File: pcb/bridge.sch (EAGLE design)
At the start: 37 parts, among them IC1 MEGA8-AI, IC4 78L05SMD, IC5 LM358D

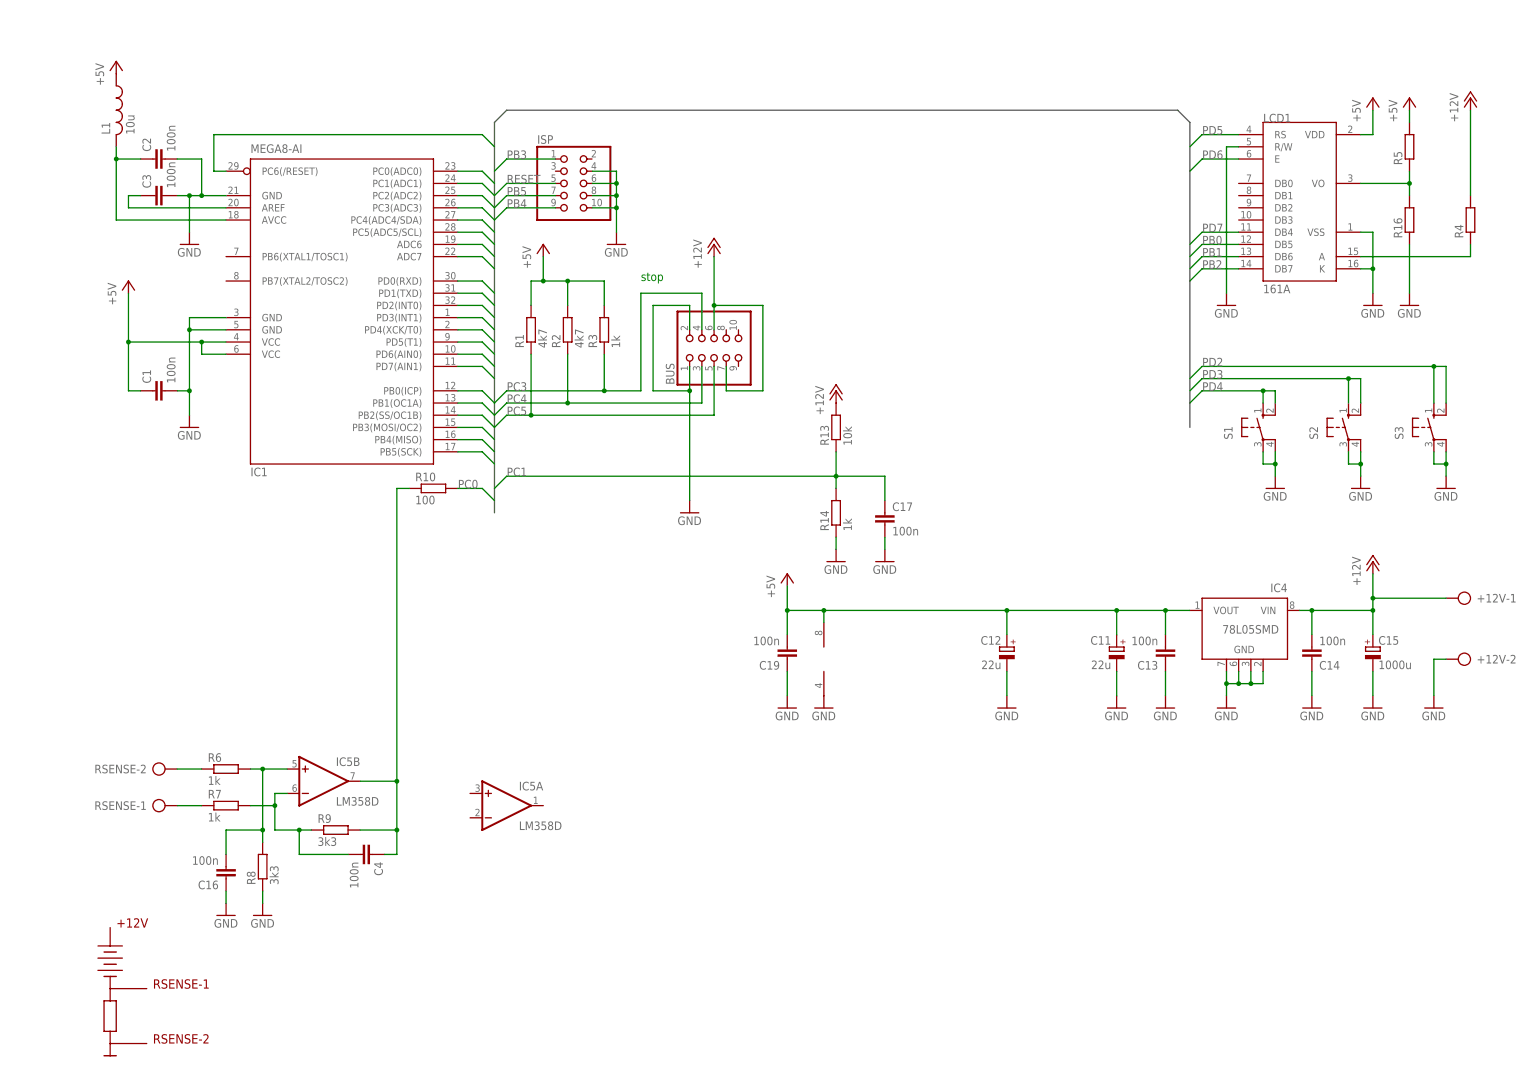
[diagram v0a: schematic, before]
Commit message: Bridge USB schematic.
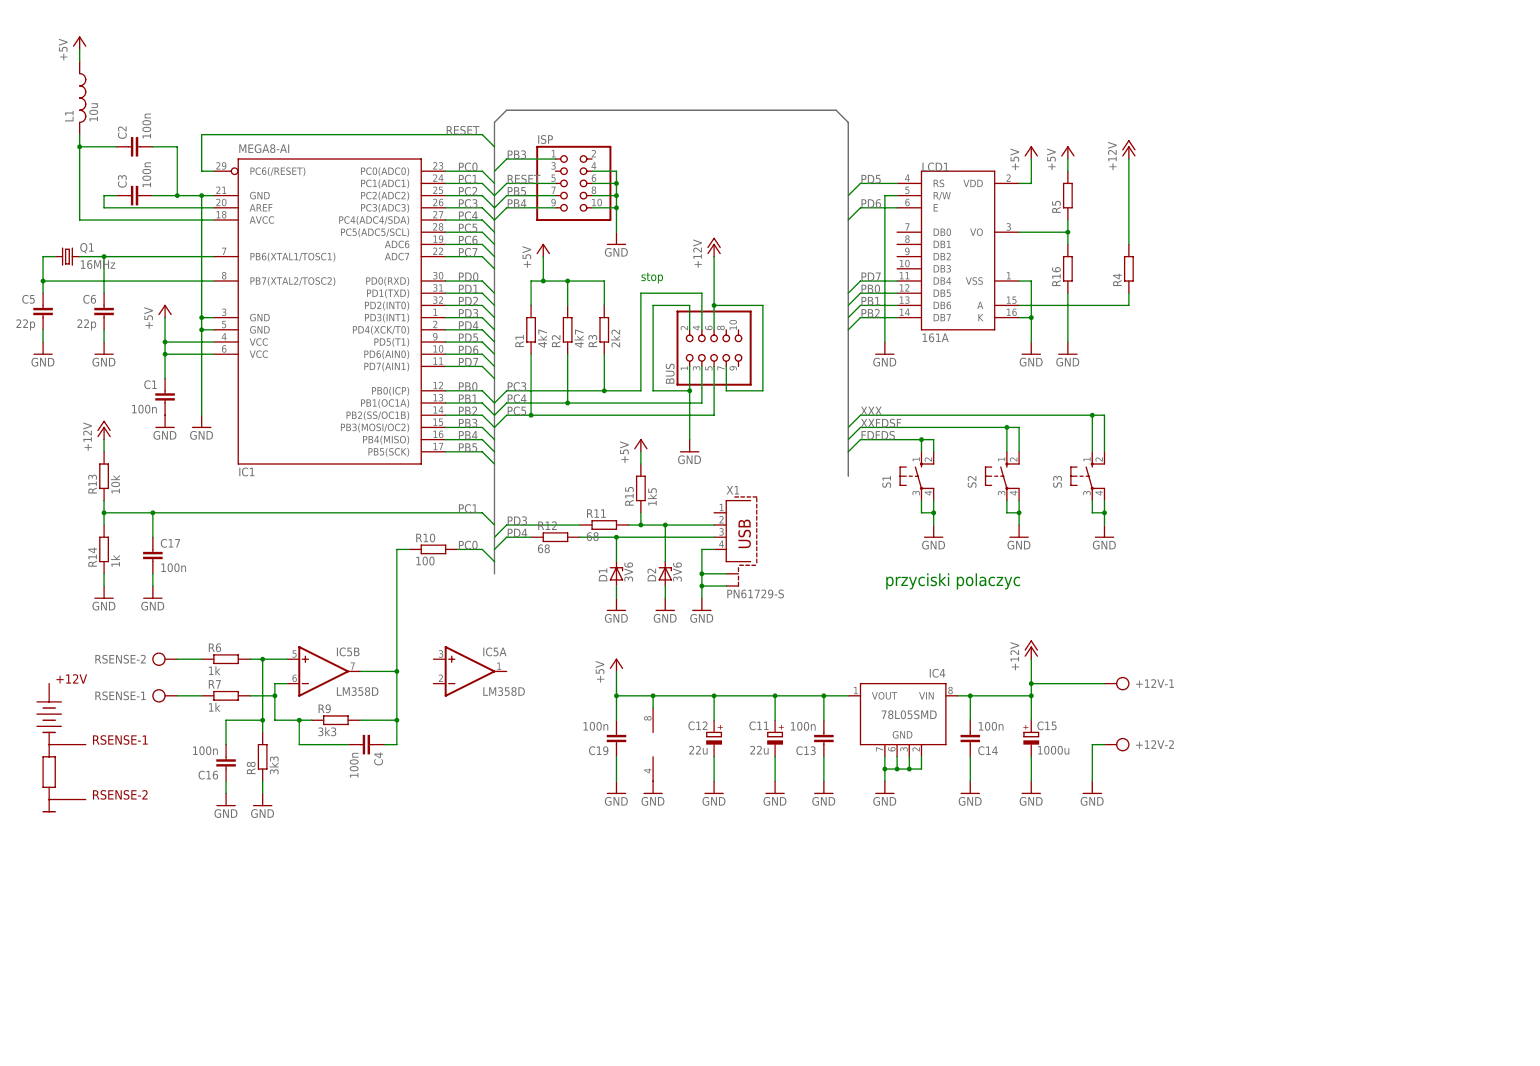
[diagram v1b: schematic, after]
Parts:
- added C5, C6: 22p, rcl:C-EUC1206
- added D1, D2: 3V6, diode:ZENER-DIODEDO34-7
- added Q1: 16MHz, crystal:CRYSTALHC49UP
- added R11, R12: 68, rcl:R-EU_M1206
- added R15: 1k5, rcl:R-EU_M1206
- added X1: PN61729-S, con-berg:PN61729-S
- R3: value 1k -> 2k2
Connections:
- new net FDFDS: S1.S, S1.S1
- new net N$11: C5.1, IC1.PB7(XTAL2/TOSC2), Q1.1
- new net N$5: D2.C, R11.2, R15.1, X1.2
- new net N$6: D1.C, R12.2, X1.3
- new net N$9: C6.1, IC1.PB6(XTAL1/TOSC1), Q1.2
- new net XXFDSF: S2.S, S2.S1
- new net XXX: S3.S, S3.S1
- net +5V: now also R15.2
- net GND: now also C5.2, C6.2, D1.A, D2.A, X1.4, X1.S1, X1.S2
- net PD2: no longer S3.S, S3.S1
- net PD3: now also R11.1; no longer S2.S, S2.S1
- net PD4: now also R12.1; no longer S1.S, S1.S1
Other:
- note added: "przyciski polaczyc"
- moved on the sheet: +12V-1, +12V-2, C1, C11, C12, C13, C14, C15, C16, C17, C19, C2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

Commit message: Bridge board ready.
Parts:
- removed C17: 100n, rcl:C-EUC1210
- added C7: 100n, rcl:C-EUC1206
- R4: device rcl:R-EU_R1218 -> rcl:R-EU_0207/12
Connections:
- removed net FDFDS: S1.S, S1.S1
- removed net XXFDSF: S2.S, S2.S1
- removed net XXX: S3.S, S3.S1
- net GND: now also C7.2; no longer C17.2
- net PC1: now also C7.1; no longer C17.1
- net PD0: now also S1.S, S1.S1
- net PD1: now also S2.S, S2.S1
- net PD2: now also S3.S, S3.S1
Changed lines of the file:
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@@
 <part name="GND13" library="supply1" deviceset="GND" device=""/>
 <part name="P+7" library="supply1" deviceset="+12V" device=""/>
-<part name="R4" library="rcl" deviceset="R-EU_" device="R1218"/>
 <part name="L1" library="rcl" deviceset="L-US" device="L1812" value="10u"/>
 <part name="IC4" library="linear" deviceset="78L*SMD" device="" technology="05"/>
@@
 <part name="P+8" library="supply1" deviceset="+5V" device=""/>
 <part name="C4" library="rcl" deviceset="C-EU" device="C1206" value="100n"/>
-<part name="C17" library="rcl" deviceset="C-EU" device="C1210" value="100n"/>
 <part name="GND5" library="supply1" deviceset="GND" device=""/>
 <part name="D1" library="diode" deviceset="ZENER-DIODE" device="DO34-7" value="3V6"/>
@@
 <part name="GND22" library="supply1" deviceset="GND" device=""/>
 <part name="GND8" library="supply1" deviceset="GND" device=""/>
+<part name="R4" library="rcl" deviceset="R-EU_" device="0207/12"/>
+<part name="C7" library="rcl" deviceset="C-EU" device="C1206" value="100n"/>
 </parts>
 <sheets>
@@
 <instance part="GND13" gate="1" x="208.28" y="0"/>
 <instance part="P+7" gate="1" x="213.36" y="81.28"/>
-<instance part="R4" gate="G$1" x="213.36" y="55.88" rot="R90"/>
 <instance part="L1" gate="G$1" x="-5.08" y="91.44"/>
 <instance part="IC4" gate="G$1" x="167.64" y="-33.02" rot="MR0"/>
@@
 <instance part="P+8" gate="1" x="200.66" y="81.28"/>
 <instance part="C4" gate="G$1" x="55.88" y="-43.18" rot="R270"/>
-<instance part="C17" gate="G$1" x="10.16" y="-2.54"/>
 <instance part="GND5" gate="1" x="10.16" y="-12.7"/>
 <instance part="D1" gate="G$1" x="106.68" y="-7.62" rot="R90"/>
@@
 <instance part="GND22" gate="1" x="0" y="38.1"/>
 <instance part="GND8" gate="1" x="12.7" y="22.86"/>
+<instance part="R4" gate="G$1" x="213.36" y="55.88" rot="R90"/>
+<instance part="C7" gate="G$1" x="10.16" y="-2.54"/>
 </instances>
 <busses>
@@
 <segment>
 <wire x1="10.16" y1="-7.62" x2="10.16" y2="-10.16" width="0.1524" layer="91"/>
-<pinref part="C17" gate="G$1" pin="2"/>
 <pinref part="GND5" gate="1" pin="GND"/>
+<pinref part="C7" gate="G$1" pin="2"/>
 </segment>
 <segment>
@@
 <wire x1="81.28" y1="2.54" x2="78.74" y2="5.08" width="0.1524" layer="91"/>
 <label x="73.66" y="5.08" size="1.778" layer="95"/>
-<pinref part="C17" gate="G$1" pin="1"/>
 <wire x1="10.16" y1="5.08" x2="10.16" y2="0" width="0.1524" layer="91"/>
 <pinref part="R13" gate="G$1" pin="1"/>
@@
 <wire x1="10.16" y1="5.08" x2="78.74" y2="5.08" width="0.1524" layer="91"/>
 <junction x="10.16" y="5.08"/>
+<pinref part="C7" gate="G$1" pin="1"/>
 </segment>
 </net>
@@
 <label x="73.66" y="53.34" size="1.778" layer="95"/>
 </segment>
+<segment>
+<wire x1="170.18" y1="17.78" x2="170.18" y2="20.32" width="0.1524" layer="91"/>
+<wire x1="170.18" y1="20.32" x2="172.72" y2="20.32" width="0.1524" layer="91"/>
+<wire x1="172.72" y1="20.32" x2="172.72" y2="17.78" width="0.1524" layer="91"/>
+<wire x1="170.18" y1="20.32" x2="157.48" y2="20.32" width="0.1524" layer="91"/>
+<wire x1="154.94" y1="17.78" x2="157.48" y2="20.32" width="0.1524" layer="91"/>
+<junction x="170.18" y="20.32"/>
+<label x="157.48" y="20.32" size="1.778" layer="95"/>
+<pinref part="S1" gate="1" pin="S"/>
+<pinref part="S1" gate="1" pin="S1"/>
+</segment>
 </net>
 <net name="PD1" class="0">
@@
 <label x="73.66" y="50.8" size="1.778" layer="95"/>
 </segment>
+<segment>
+<wire x1="190.5" y1="17.78" x2="190.5" y2="22.86" width="0.1524" layer="91"/>
+<wire x1="190.5" y1="22.86" x2="187.96" y2="22.86" width="0.1524" layer="91"/>
+<wire x1="187.96" y1="22.86" x2="187.96" y2="17.78" width="0.1524" layer="91"/>
+<wire x1="187.96" y1="22.86" x2="157.48" y2="22.86" width="0.1524" layer="91"/>
+<wire x1="154.94" y1="20.32" x2="157.48" y2="22.86" width="0.1524" layer="91"/>
+<junction x="187.96" y="22.86"/>
+<label x="157.48" y="22.86" size="1.778" layer="95"/>
+<pinref part="S2" gate="1" pin="S1"/>
+<pinref part="S2" gate="1" pin="S"/>
+</segment>
 </net>
 <net name="PD2" class="0">
@@
 <pinref part="IC1" gate="G$1" pin="PD2(INT0)"/>
 <label x="73.66" y="48.26" size="1.778" layer="95"/>
+</segment>
+<segment>
+<wire x1="205.74" y1="17.78" x2="205.74" y2="25.4" width="0.1524" layer="91"/>
+<wire x1="205.74" y1="25.4" x2="208.28" y2="25.4" width="0.1524" layer="91"/>
+<wire x1="208.28" y1="25.4" x2="208.28" y2="17.78" width="0.1524" layer="91"/>
+<wire x1="205.74" y1="25.4" x2="157.48" y2="25.4" width="0.1524" layer="91"/>
+<wire x1="154.94" y1="22.86" x2="157.48" y2="25.4" width="0.1524" layer="91"/>
+<junction x="205.74" y="25.4"/>
+<label x="157.48" y="25.4" size="1.778" layer="95"/>
+<pinref part="S3" gate="1" pin="S"/>
+<pinref part="S3" gate="1" pin="S1"/>
 </segment>
 </net>
@@
 </segment>
 </net>
-<net name="XXX" class="0">
-<segment>
-<wire x1="205.74" y1="17.78" x2="205.74" y2="25.4" width="0.1524" layer="91"/>
-<wire x1="205.74" y1="25.4" x2="208.28" y2="25.4" width="0.1524" layer="91"/>
-<wire x1="208.28" y1="25.4" x2="208.28" y2="17.78" width="0.1524" layer="91"/>
-<wire x1="205.74" y1="25.4" x2="157.48" y2="25.4" width="0.1524" layer="91"/>
-<wire x1="154.94" y1="22.86" x2="157.48" y2="25.4" width="0.1524" layer="91"/>
-<junction x="205.74" y="25.4"/>
-<label x="157.48" y="25.4" size="1.778" layer="95"/>
-<pinref part="S3" gate="1" pin="S"/>
-<pinref part="S3" gate="1" pin="S1"/>
-</segment>
-</net>
-<net name="XXFDSF" class="0">
-<segment>
-<wire x1="190.5" y1="17.78" x2="190.5" y2="22.86" width="0.1524" layer="91"/>
-<wire x1="190.5" y1="22.86" x2="187.96" y2="22.86" width="0.1524" layer="91"/>
-<wire x1="187.96" y1="22.86" x2="187.96" y2="17.78" width="0.1524" layer="91"/>
-<wire x1="187.96" y1="22.86" x2="157.48" y2="22.86" width="0.1524" layer="91"/>
-<wire x1="154.94" y1="20.32" x2="157.48" y2="22.86" width="0.1524" layer="91"/>
-<junction x="187.96" y="22.86"/>
-<label x="157.48" y="22.86" size="1.778" layer="95"/>
-<pinref part="S2" gate="1" pin="S1"/>
-<pinref part="S2" gate="1" pin="S"/>
-</segment>
-</net>
-<net name="FDFDS" class="0">
-<segment>
-<wire x1="170.18" y1="17.78" x2="170.18" y2="20.32" width="0.1524" layer="91"/>
-<wire x1="170.18" y1="20.32" x2="172.72" y2="20.32" width="0.1524" layer="91"/>
-<wire x1="172.72" y1="20.32" x2="172.72" y2="17.78" width="0.1524" layer="91"/>
-<wire x1="170.18" y1="20.32" x2="157.48" y2="20.32" width="0.1524" layer="91"/>
-<wire x1="154.94" y1="17.78" x2="157.48" y2="20.32" width="0.1524" layer="91"/>
-<junction x="170.18" y="20.32"/>
-<label x="157.48" y="20.32" size="1.778" layer="95"/>
-<pinref part="S1" gate="1" pin="S"/>
-<pinref part="S1" gate="1" pin="S1"/>
-</segment>
-</net>
 </nets>
 </sheet>
 </sheets>
+<errors>
+</errors>
 </schematic>
 </drawing>

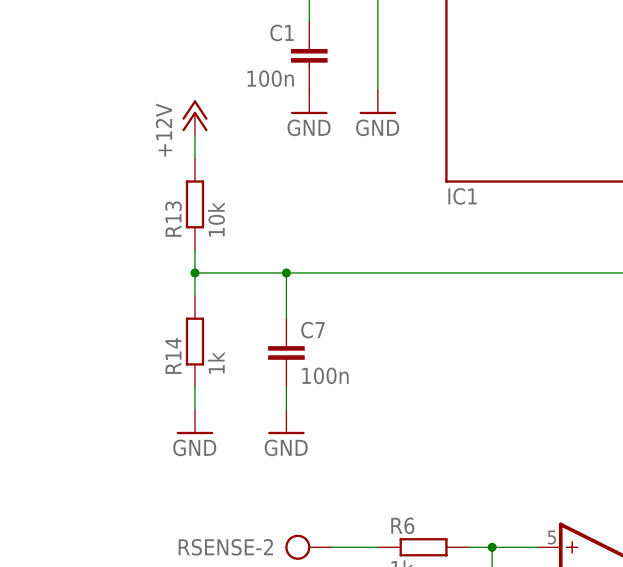
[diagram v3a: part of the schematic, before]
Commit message: Corrected bridge voltage divider to match the resistor values.
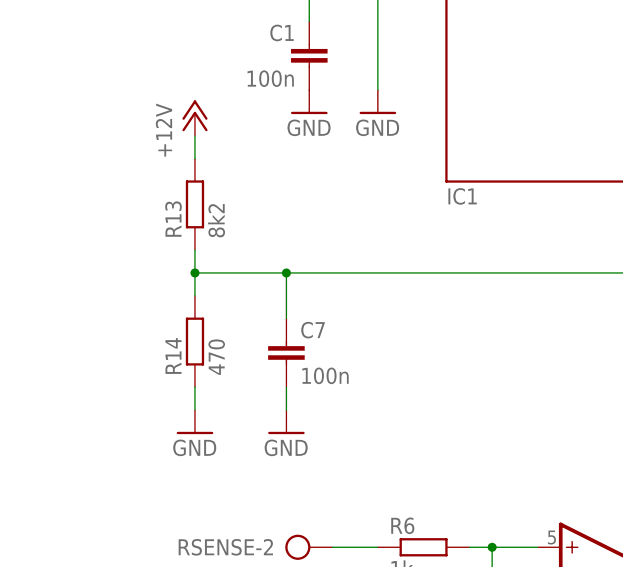
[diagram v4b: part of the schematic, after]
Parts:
- R13: value 10k -> 8k2
- R14: value 1k -> 470
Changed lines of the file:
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@@
 <part name="GND26" library="supply1" deviceset="GND" device=""/>
 <part name="R10" library="rcl" deviceset="R-EU_" device="M1206" value="100"/>
-<part name="R13" library="rcl" deviceset="R-EU_" device="M1206" value="10k"/>
+<part name="R13" library="rcl" deviceset="R-EU_" device="M1206" value="8k2"/>
 <part name="GND27" library="supply1" deviceset="GND" device=""/>
-<part name="R14" library="rcl" deviceset="R-EU_" device="M1206" value="1k"/>
+<part name="R14" library="rcl" deviceset="R-EU_" device="M1206" value="470"/>
 <part name="P+12" library="supply1" deviceset="+12V" device=""/>
 <part name="RSENSE" library="con-ptr500" deviceset="AK500/2" device=""/>
